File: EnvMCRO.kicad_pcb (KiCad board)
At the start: 2 copper layers, 109.6 x 69.7 mm, 30 parts, among them U1 Pico

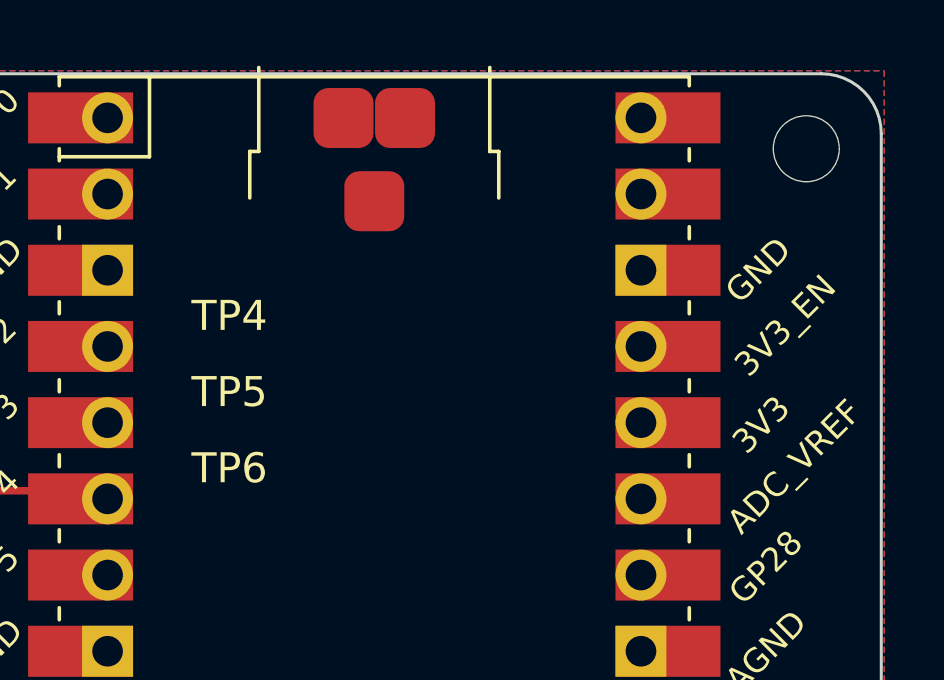
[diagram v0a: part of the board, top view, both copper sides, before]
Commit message: Removed unused pads, Added modified footprint of rpi pico
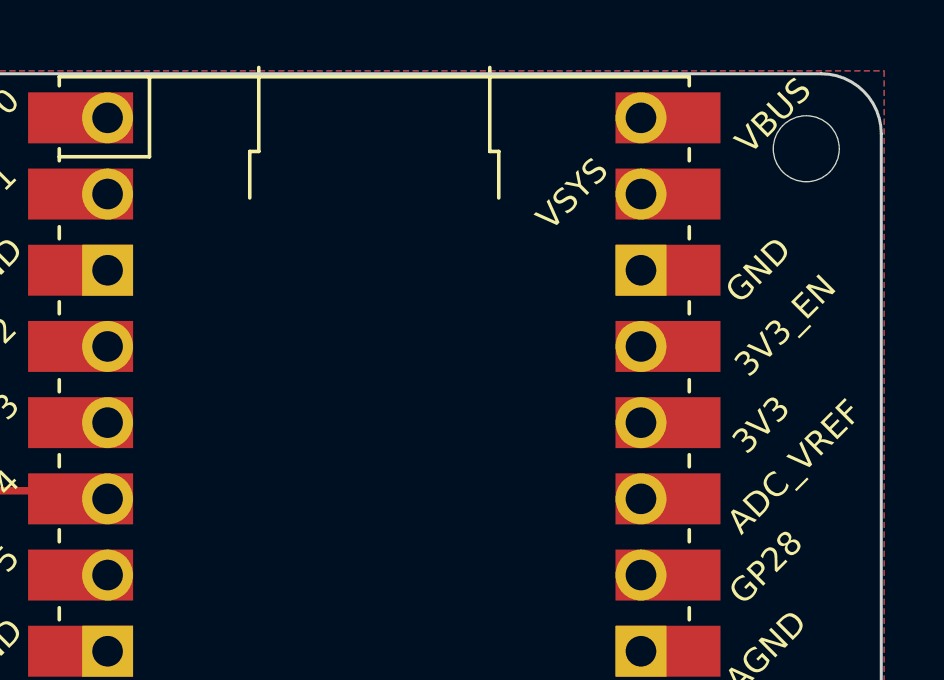
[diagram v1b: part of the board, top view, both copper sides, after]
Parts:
- U1: footprint MCU_RaspberryPi_and_Boards.pretty:RPi_Pico_SMD_TH -> Pico:RPi_Pico_SMD_TH
